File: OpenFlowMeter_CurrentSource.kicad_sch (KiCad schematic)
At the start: 20 parts, among them J1 Screw_Terminal_01x02, Q2 BC556, U1 LT1492

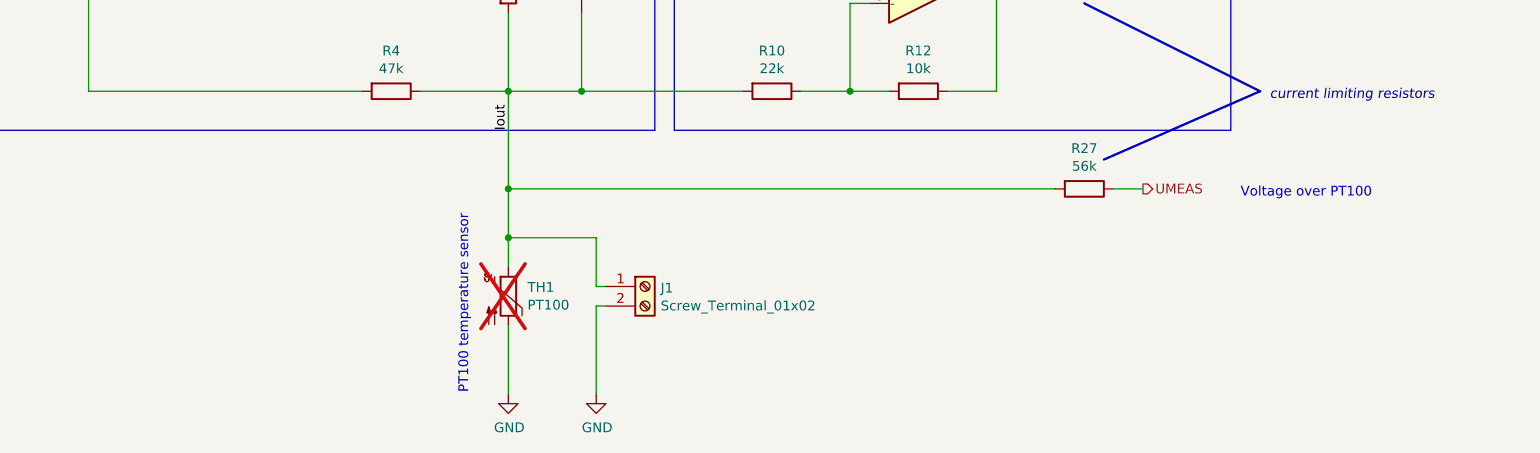
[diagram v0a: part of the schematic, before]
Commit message: changed to 3 wire PT100 connections
removed SMD PT100
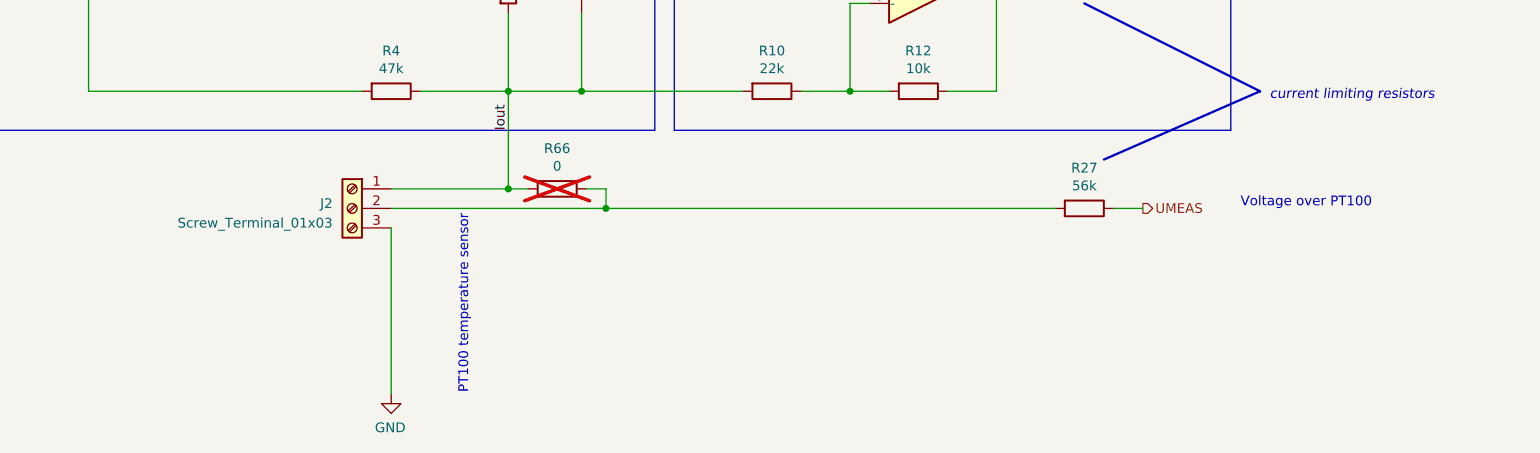
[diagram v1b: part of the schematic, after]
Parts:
- removed J1: Screw_Terminal_01x02, TerminalBlock_RND:TerminalBlock_RND_205-00232_1x02_P5.08mm_Horizontal, symbol Connector:Screw_Terminal_01x02
- removed TH1: PT100, Resistor_SMD:R_0805_2012Metric, symbol Sensor_Temperature:PT100
- added J2: Screw_Terminal_01x03, TerminalBlock_4Ucon:TerminalBlock_4Ucon_1x03_P3.50mm_Horizontal, symbol Connector:Screw_Terminal_01x03
- added R66: 0, Resistor_SMD:R_0603_1608Metric, symbol Device:R
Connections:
- net GND: now also J2.3 (Pin_3)
- net Iout: now also J2.1 (Pin_1), R66.2; no longer R27.2
- new net: J2.2 (Pin_2), R27.2, R66.1
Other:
- moved on the sheet: R27

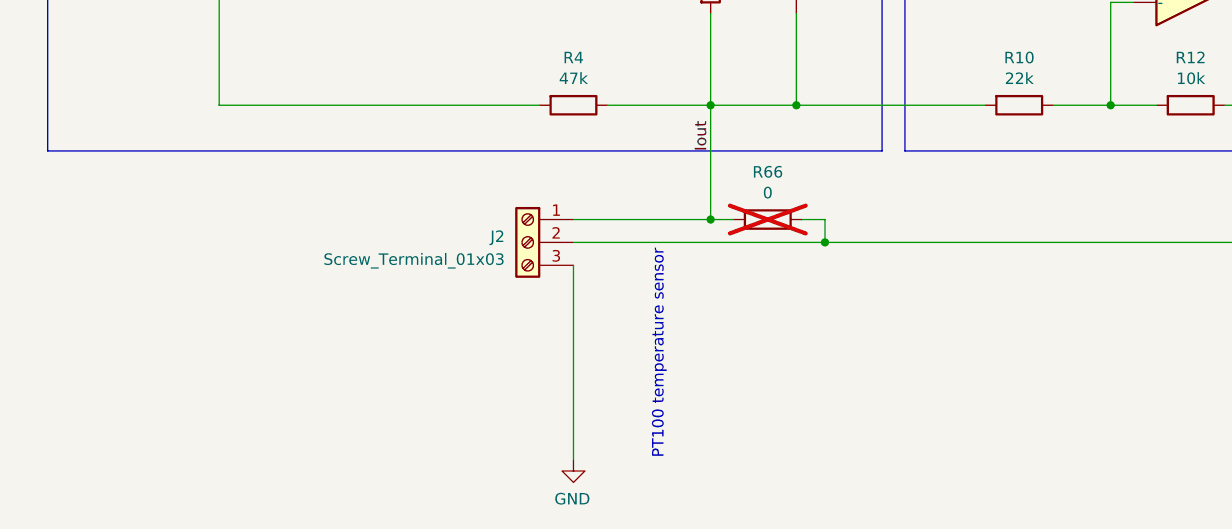
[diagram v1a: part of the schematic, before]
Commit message: implemented 3wire connection option
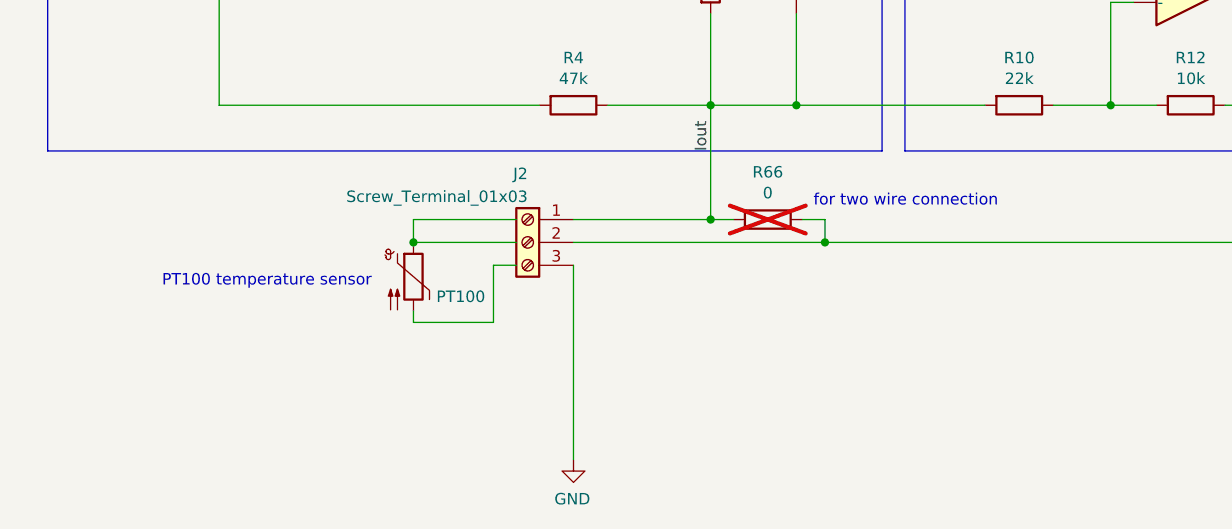
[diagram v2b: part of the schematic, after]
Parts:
- added TH2: PT100, symbol Sensor_Temperature:PT100
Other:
- note added: "for two wire connection"
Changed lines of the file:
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@@
   (junction (at 118.11 101.6) (diameter 0) (color 0 0 0 0)
+  )
+  (junction (at 85.09 144.78) (diameter 0) (color 0 0 0 0)
   )
   (junction (at 63.5 81.28) (diameter 0) (color 0 0 0 0)
@@
     (stroke (width 0) (type default))
   )
+  (wire (pts (xy 93.98 153.67) (xy 85.09 153.67))
+    (stroke (width 0) (type default))
+  )
+  (wire (pts (xy 85.09 144.78) (xy 96.52 144.78))
+    (stroke (width 0) (type default))
+  )
   (wire (pts (xy 179.07 67.31) (xy 179.07 73.66))
     (stroke (width 0) (type default))
@@
     (stroke (width 0) (type default))
   )
+  (wire (pts (xy 96.52 147.32) (xy 93.98 147.32))
+    (stroke (width 0) (type default))
+  )
   (wire (pts (xy 118.11 142.24) (xy 120.65 142.24))
     (stroke (width 0) (type default))
@@
     (stroke (width 0) (type default))
   )
+  (wire (pts (xy 96.52 142.24) (xy 85.09 142.24))
+    (stroke (width 0) (type default))
+  )
+  (wire (pts (xy 85.09 153.67) (xy 85.09 152.4))
+    (stroke (width 0) (type default))
+  )
   (wire (pts (xy 54.61 81.28) (xy 63.5 81.28))
     (stroke (width 0) (type default))
@@
   )
   (wire (pts (xy 118.11 66.04) (xy 118.11 64.77))
+    (stroke (width 0) (type default))
+  )
+  (wire (pts (xy 93.98 147.32) (xy 93.98 153.67))
     (stroke (width 0) (type default))
   )
@@
     (stroke (width 0) (type default))
   )
+  (wire (pts (xy 85.09 142.24) (xy 85.09 144.78))
+    (stroke (width 0) (type default))
+  )
   (polyline (pts (xy 137.16 134.62) (xy 44.45 134.62))
     (stroke (width 0) (type default))
@@
   (wire (pts (xy 162.56 101.6) (xy 162.56 113.03))
     (stroke (width 0) (type default))
+  )
+  (text "for two wire connection" (at 129.54 140.97 0)
+    (effects (font (size 1.27 1.27)) (justify left bottom))
   )
   (text "Voltage over PT100" (at 213.36 144.78 0)
@@
     (effects (font (size 1.27 1.27)) (justify left bottom))
   )
-  (text "PT100 temperature sensor" (at 113.03 168.91 90)
+  (text "PT100 temperature sensor" (at 57.15 149.86 0)
     (effects (font (size 1.27 1.27)) (justify left bottom))
   )
@@
     )
   )
+  (symbol (lib_id "Sensor_Temperature:PT100") (at 85.09 148.59 0) (unit 1)
+    (in_bom no) (on_board no) (dnp no) (fields_autoplaced)
+    (property "Reference" "TH2" (at 87.63 148.2725 0)
+      (effects (font (size 1.27 1.27)) (justify left) hide)
+    )
+    (property "Value" "PT100" (at 87.63 150.8125 0)
+      (effects (font (size 1.27 1.27)) (justify left))
+    )
+    (property "Footprint" "" (at 85.09 147.32 0)
+      (effects (font (size 1.27 1.27)) hide)
+    )
+    (property "Datasheet" "https://www.heraeus.com/media/media/group/doc_group/products_1/hst/sot_to/de_15/to_92_d.pdf" (at 85.09 147.32 0)
+      (effects (font (size 1.27 1.27)) hide)
+    )
+    (pin "1")
+    (pin "2")
+    (instances
+      (project "OpenFlowMeter"
+        (path "/25e5aa8e-2696-44a3-8d3c-c2c53f2923cf/00000000-0000-0000-0000-00006065743c"
+          (reference "TH2") (unit 1)
+        )
+        (path "/25e5aa8e-2696-44a3-8d3c-c2c53f2923cf/00000000-0000-0000-0000-00006062503a"
+          (reference "TH1") (unit 1)
+        )
+      )
+    )
+  )
   (symbol (lib_id "Device:R") (at 193.04 115.57 270) (unit 1)
     (in_bom yes) (on_board yes) (dnp no)
@@
   (symbol (lib_id "Connector:Screw_Terminal_01x03") (at 97.79 144.78 0) (mirror y) (unit 1)
     (in_bom yes) (on_board yes) (dnp no)
-    (property "Reference" "J2" (at 95.25 144.145 0)
-      (effects (font (size 1.27 1.27)) (justify left))
-    )
-    (property "Value" "Screw_Terminal_01x03" (at 95.25 146.685 0)
-      (effects (font (size 1.27 1.27)) (justify left))
-    )
+    (property "Reference" "J2" (at 97.79 137.16 0)
+      (effects (font (size 1.27 1.27)) (justify left))
+    )
+    (property "Value" "Screw_Terminal_01x03" (at 97.79 139.7 0)
+      (effects (font (size 1.27 1.27)) (justify left))
+    )

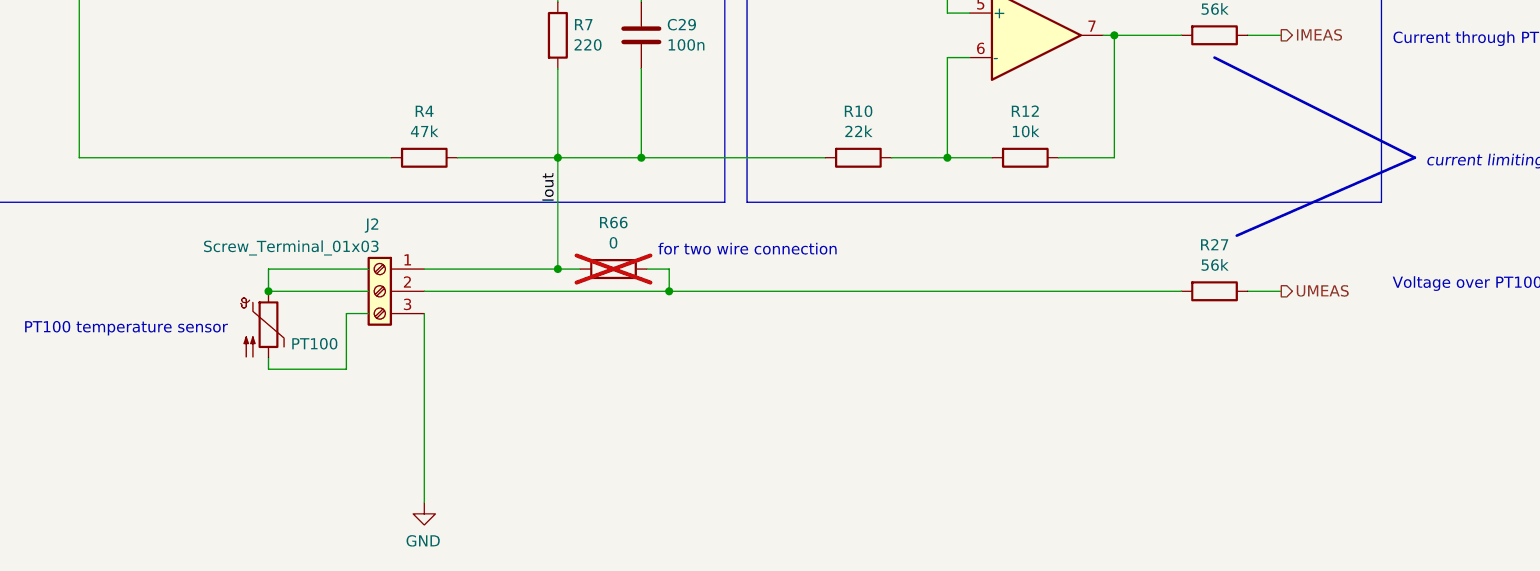
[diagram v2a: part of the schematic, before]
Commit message: updated connector to 1x4
this allows 4 wire connection of the PT100.
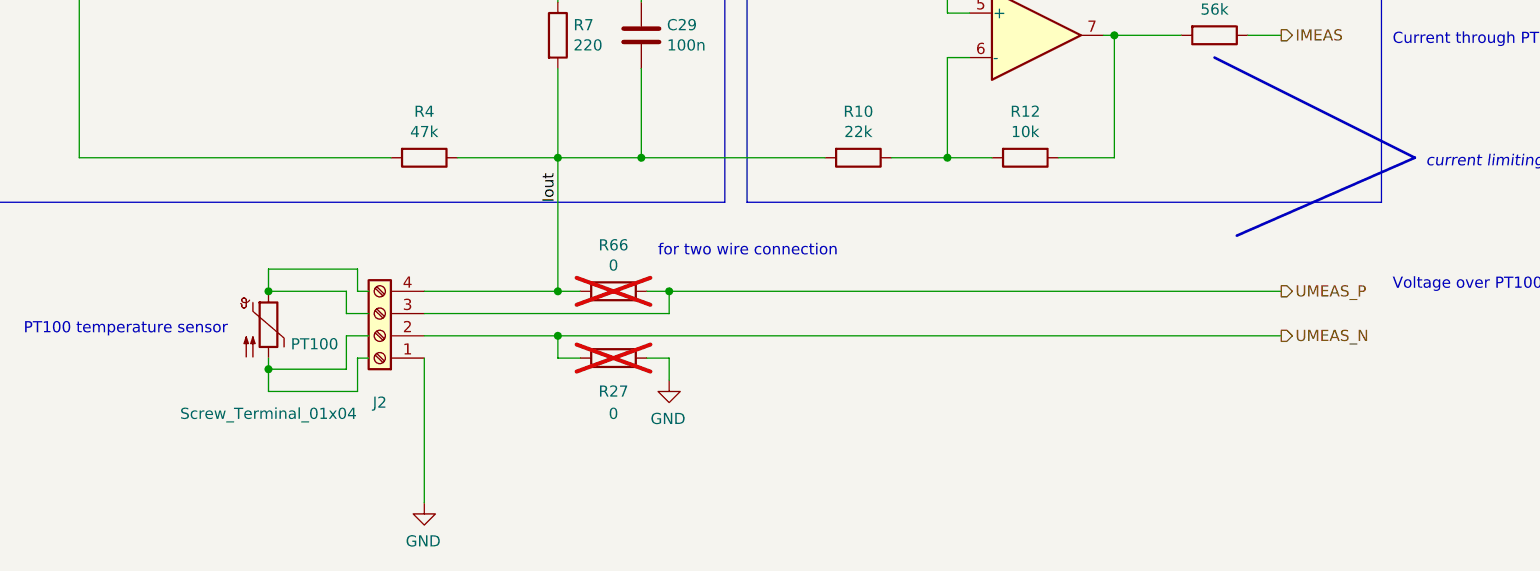
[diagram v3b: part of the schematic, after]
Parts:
- removed J2: Screw_Terminal_01x03, TerminalBlock_4Ucon:TerminalBlock_4Ucon_1x03_P3.50mm_Horizontal, symbol Connector:Screw_Terminal_01x03
- added J2: Screw_Terminal_01x04, Connector_Wago:Wago_733-364_1x04_P2.50mm_Horizontal, symbol Connector:Screw_Terminal_01x04
- R27: value 56k -> 0; now not fitted
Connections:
- net UMEAS is gone; now on net GND: R27.1
- net GND: now also J2.1 (Pin_1)
- net Iout: now also J2.4 (Pin_4)
- net UMEAS_N: now reaches R27.2
- net UMEAS_N: now also J2.2 (Pin_2); no longer R66.1
- new net UMEAS_P: J2.3 (Pin_3), R66.1
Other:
- moved on the sheet: R66

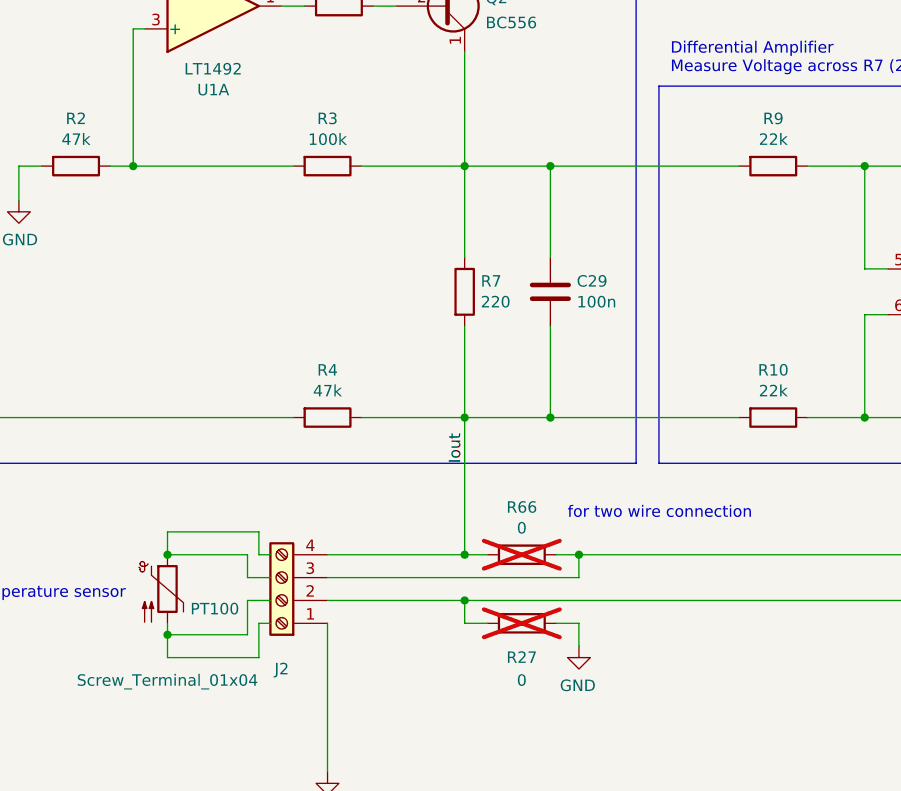
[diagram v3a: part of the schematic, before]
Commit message: had to push some symbols and lines to the grid for ERC clean
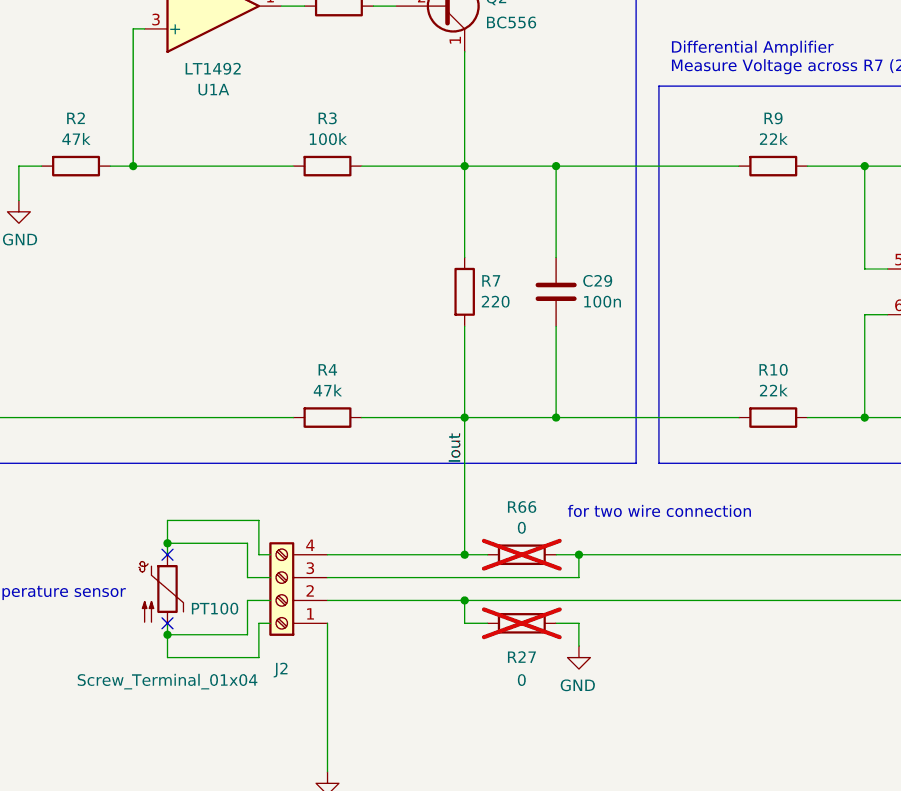
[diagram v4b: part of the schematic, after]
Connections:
- no-connect marks 0 -> 2
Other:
- moved on the sheet: C29
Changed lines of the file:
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@@
   (junction (at 118.11 101.6) (diameter 0) (color 0 0 0 0)
   )
-  (junction (at 85.09 144.78) (diameter 0) (color 0 0 0 0)
-  )
   (junction (at 63.5 81.28) (diameter 0) (color 0 0 0 0)
   )
   (junction (at 162.56 101.6) (diameter 0) (color 0 0 0 0)
   )
-  (junction (at 127.635 101.6) (diameter 0) (color 0 0 0 0)
-  )
-  (junction (at 127.635 129.54) (diameter 0) (color 0 0 0 0)
+  (junction (at 128.27 101.6) (diameter 0) (color 0 0 0 0)
+  )
+  (junction (at 128.27 129.54) (diameter 0) (color 0 0 0 0)
   )
   (junction (at 81.28 101.6) (diameter 0) (color 0 0 0 0)
@@
   (junction (at 130.81 144.78) (diameter 0) (color 0 0 0 0)
   )
+  (junction (at 85.09 143.51) (diameter 0) (color 0 0 0 0)
+  )
   (junction (at 162.56 129.54) (diameter 0) (color 0 0 0 0)
   )
+  (no_connect (at 85.09 144.78))
+  (no_connect (at 85.09 152.4))
   (wire (pts (xy 96.52 144.78) (xy 95.25 144.78))
     (stroke (width 0) (type default))
@@
     (stroke (width 0) (type default))
   )
-  (wire (pts (xy 93.98 144.78) (xy 93.98 147.32))
+  (wire (pts (xy 93.98 143.51) (xy 93.98 147.32))
     (stroke (width 0) (type default))
   )
@@
     (stroke (width 0) (type default))
   )
-  (wire (pts (xy 148.59 101.6) (xy 127.635 101.6))
+  (wire (pts (xy 148.59 101.6) (xy 128.27 101.6))
     (stroke (width 0) (type default))
   )
@@
     (stroke (width 0) (type default))
   )
-  (wire (pts (xy 85.09 144.78) (xy 93.98 144.78))
+  (wire (pts (xy 85.09 143.51) (xy 93.98 143.51))
     (stroke (width 0) (type default))
   )
@@
     (stroke (width 0) (type default))
   )
-  (wire (pts (xy 95.25 142.24) (xy 85.09 142.24))
+  (wire (pts (xy 95.25 140.97) (xy 85.09 140.97))
     (stroke (width 0) (type default))
   )
@@
     (stroke (width 0) (type default))
   )
-  (wire (pts (xy 127.635 101.6) (xy 127.635 111.76))
+  (wire (pts (xy 128.27 101.6) (xy 128.27 111.76))
     (stroke (width 0) (type default))
   )
@@
     (stroke (width 0) (type default))
   )
-  (wire (pts (xy 127.635 129.54) (xy 148.59 129.54))
+  (wire (pts (xy 128.27 129.54) (xy 148.59 129.54))
     (stroke (width 0) (type default))
   )
@@
     (stroke (width 0) (type default))
   )
-  (wire (pts (xy 127.635 119.38) (xy 127.635 129.54))
+  (wire (pts (xy 128.27 119.38) (xy 128.27 129.54))
     (stroke (width 0) (type default))
   )
@@
     (stroke (width 0) (type default))
   )
-  (wire (pts (xy 118.11 129.54) (xy 127.635 129.54))
+  (wire (pts (xy 118.11 129.54) (xy 128.27 129.54))
     (stroke (width 0) (type default))
   )
@@
     (stroke (width 0) (type default))
   )
-  (wire (pts (xy 85.09 142.24) (xy 85.09 144.78))
+  (wire (pts (xy 85.09 140.97) (xy 85.09 143.51))
     (stroke (width 0) (type default))
   )
@@
     (stroke (width 0) (type default))
   )
-  (wire (pts (xy 127.635 101.6) (xy 118.11 101.6))
+  (wire (pts (xy 128.27 101.6) (xy 118.11 101.6))
     (stroke (width 0) (type default))
   )
@@
     (stroke (width 0) (type default))
   )
-  (wire (pts (xy 95.25 142.24) (xy 95.25 144.78))
+  (wire (pts (xy 95.25 140.97) (xy 95.25 144.78))
     (stroke (width 0) (type default))
   )
@@
   )
   (wire (pts (xy 130.81 147.32) (xy 130.81 144.78))
+    (stroke (width 0) (type default))
+  )
+  (wire (pts (xy 85.09 143.51) (xy 85.09 144.78))
     (stroke (width 0) (type default))
   )
@@
       (effects (font (size 1.27 1.27)) hide)
     )
+    (property "Sim.Enable" "0" (at 85.09 148.59 0)
+      (effects (font (size 1.27 1.27)) hide)
+    )
     (pin "1")
     (pin "2")
@@
     )
   )
-  (symbol (lib_id "Device:C") (at 127.635 115.57 0) (unit 1)
-    (in_bom yes) (on_board yes) (dnp no)
-    (property "Reference" "C29" (at 130.556 114.4016 0)
-      (effects (font (size 1.27 1.27)) (justify left))
-    )
-    (property "Value" "100n" (at 130.556 116.713 0)
-      (effects (font (size 1.27 1.27)) (justify left))
-    )
-    (property "Footprint" "Capacitor_SMD:C_0603_1608Metric" (at 128.6002 119.38 0)
-      (effects (font (size 1.27 1.27)) hide)
-    )
-    (property "Datasheet" "~" (at 127.635 115.57 0)
-      (effects (font (size 1.27 1.27)) hide)
-    )
+  (symbol (lib_id "Device:C") (at 128.27 115.57 0) (unit 1)
+    (in_bom yes) (on_board yes) (dnp no)
+    (property "Reference" "C29" (at 131.191 114.4016 0)
+      (effects (font (size 1.27 1.27)) (justify left))
+    )
+    (property "Value" "100n" (at 131.191 116.713 0)
+      (effects (font (size 1.27 1.27)) (justify left))
+    )
+    (property "Footprint" "Capacitor_SMD:C_0603_1608Metric" (at 129.2352 119.38 0)
+      (effects (font (size 1.27 1.27)) hide)
+    )
+    (property "Datasheet" "~" (at 128.27 115.57 0)
+      (effects (font (size 1.27 1.27)) hide)
+    )
